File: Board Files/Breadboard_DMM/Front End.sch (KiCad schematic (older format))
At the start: 35 parts

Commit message: Started cleaning up front end page
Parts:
- removed C?: 1uF, symbol Device:C
- removed R?: 10k, symbol Device:R_US
- removed U?: 74VHC4052AFT, Package_SO:TSSOP-16_4.4x5mm_P0.65mm, symbol irex_Analog_Switch:74VHC4052AFT
- K? (x8): symbol irex_Relay:EC2-5NU_separated -> irex_Relay:EC2-5NU_Split
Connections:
- net labels added: CURRENT_SOURCE_ON, METER_CURRENT_SOURCE
- net labels removed: OHMETER_CURRENT_SOURCE, OHMETER_ON
- wire segments 134 -> 110
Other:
- note added: "Input divider"
- note removed: "0"
- note removed: "1"
- note removed: "4.096V"
- note removed: "A"
- note removed: "B\n"
- note removed: "Calibration Mux"
- note removed: "Connection"
- note removed: "GND"
- note removed: "Inputs Shorted"
- note removed: "Voltmeter \ninput divider"
- moved on the sheet: D?, R?, U?B

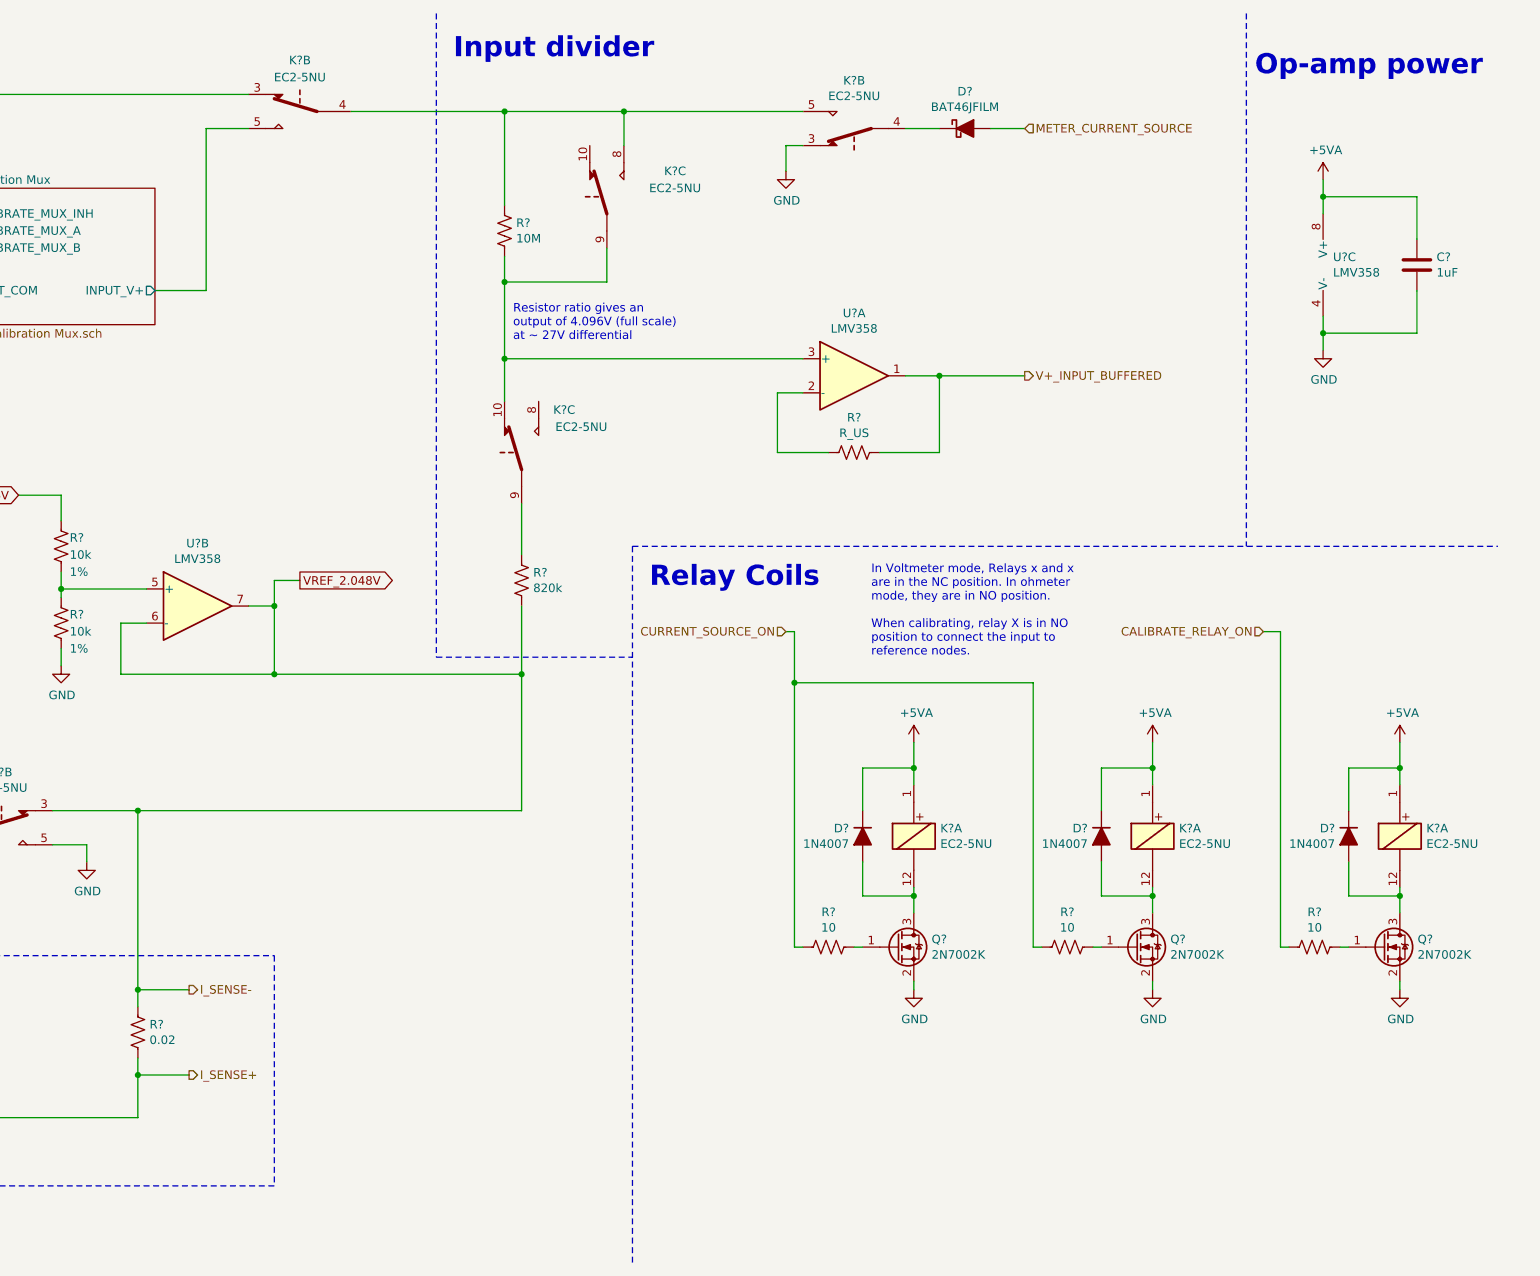
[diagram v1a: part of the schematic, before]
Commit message: Starting converting to hierachichal design
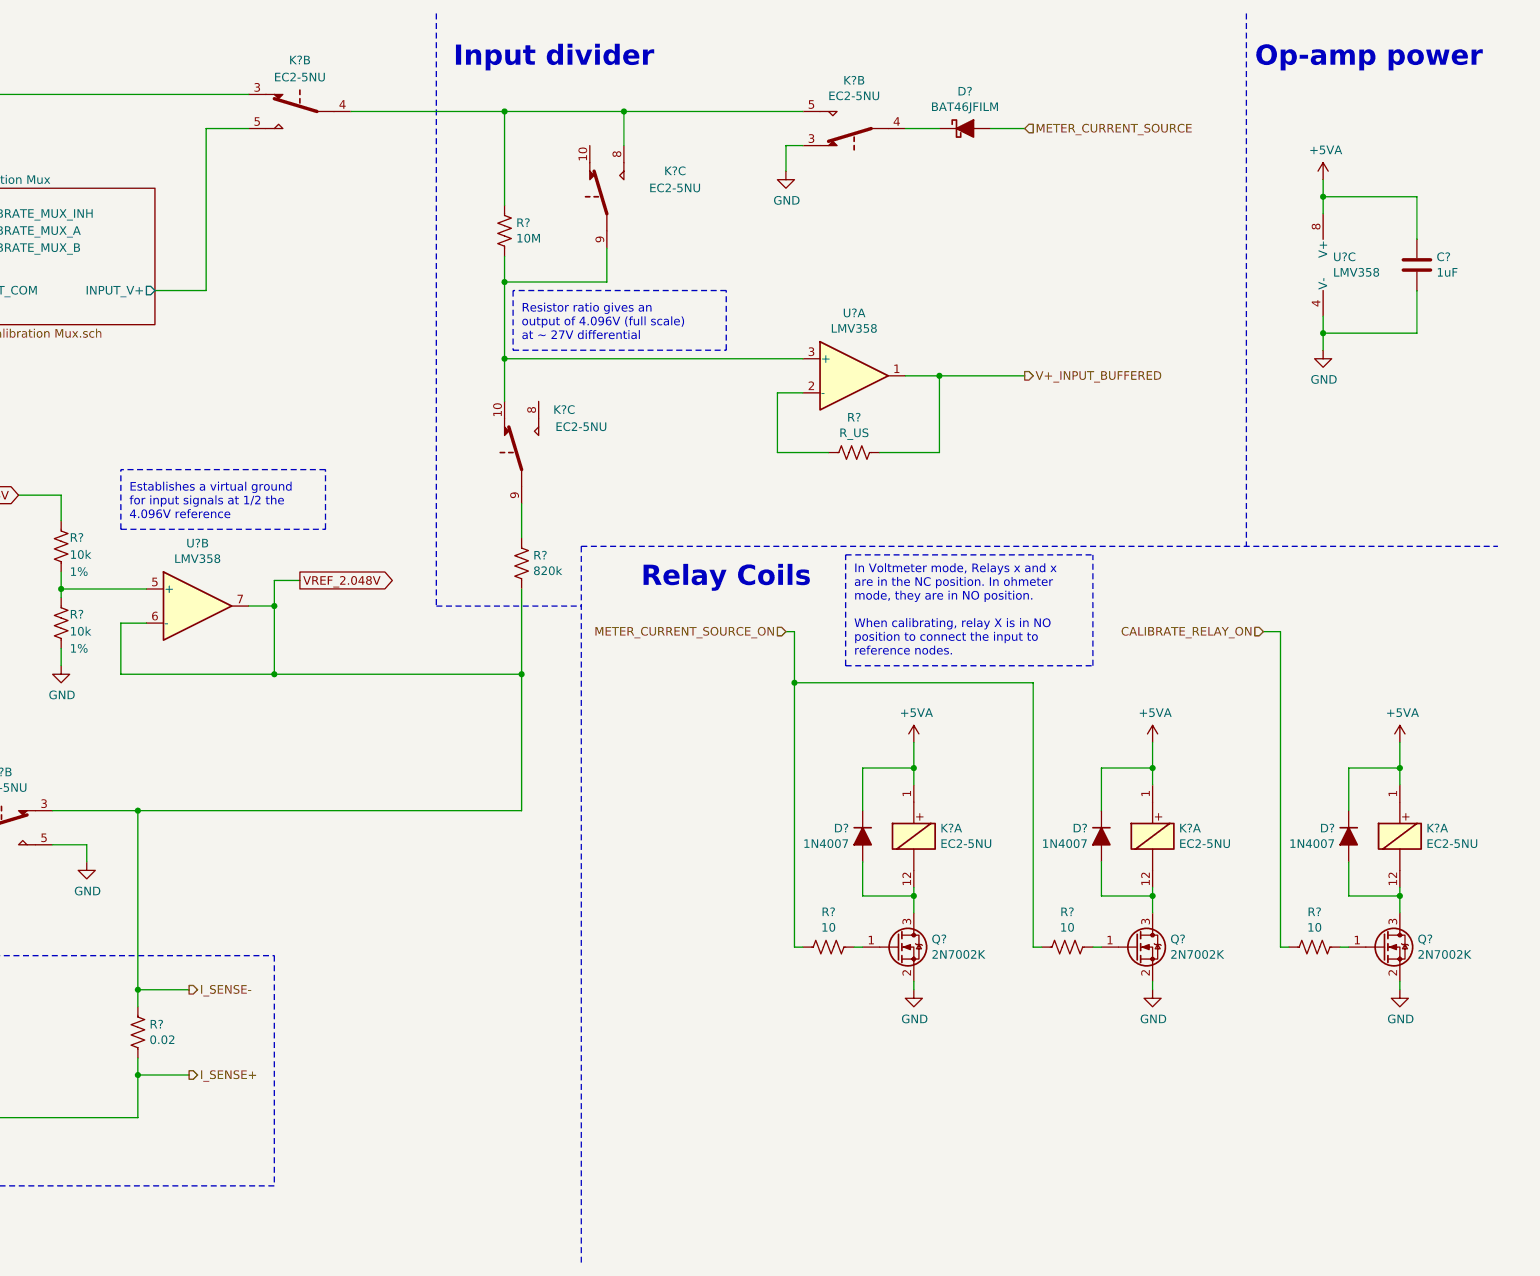
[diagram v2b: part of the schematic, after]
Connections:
- net CURRENT_SOURCE_ON renamed METER_CURRENT_SOURCE_ON
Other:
- note added: "Establishes a virtual ground \nfor input signals at 1/2 the \n4.096V reference\n"
- moved on the sheet: R?
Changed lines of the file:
@@
 $Descr A4 11693 8268
 encoding utf-8
-Sheet 2 6
+Sheet 4 6
 Title ""
 Date ""
@@
 	1    0    0    -1
 $EndComp
-Text Notes 5450 2400 0    50   ~ 0
+Text Notes 5500 2400 0    50   ~ 0
 Resistor ratio gives an \noutput of 4.096V (full scale)\nat ~~ 27V differential
 $Comp
 L Device:R_US R?
 U 1 1 5F569319
-P 5500 3800
+P 5500 3700
 AR Path="/5F569319" Ref="R?"  Part="1"
 AR Path="/5F511849/5F569319" Ref="R?"  Part="1"
-F 0 "R?" H 5568 3846 50  0000 L CNN
-F 1 "820k" H 5568 3755 50  0000 L CNN
-F 2 "" V 5540 3790 50  0001 C CNN
-F 3 "~" H 5500 3800 50  0001 C CNN
-	1    5500 3800
+F 0 "R?" H 5568 3746 50  0000 L CNN
+F 1 "820k" H 5568 3655 50  0000 L CNN
+F 2 "" V 5540 3690 50  0001 C CNN
+F 3 "~" H 5500 3700 50  0001 C CNN
+	1    5500 3700
 	1    0    0    -1
 $EndComp
@@
 $EndComp
 Wire Wire Line
-	5500 3950 5500 4350
+	5500 3850 5500 4350
 Wire Wire Line
 	2750 5150 3250 5150
@@
 	2950 5350 2950 5450
 Wire Wire Line
-	5500 3650 5500 3350
+	5500 3550 5500 3350
 Wire Wire Line
 	5400 2750 5400 2500
@@
 Connection ~ 7950 2600
 Wire Notes Line
-	6150 3600 11225 3600
+	5850 3600 11225 3600
 Wire Notes Line
 	9750 475  9750 3600
-Text Notes 9800 850  0    118  ~ 24
+Text Notes 9800 800  0    118  ~ 24
 Op-amp power\n
-Text Notes 6250 3850 0    118  ~ 24
+Text Notes 6200 3850 0    118  ~ 24
 Relay Coils
 Wire Notes Line
@@
 Connection ~ 3250 6200
 Connection ~ 3250 5150
-Text Notes 7550 4250 0    50   ~ 0
+Text Notes 7450 4250 0    50   ~ 0
 In Voltmeter mode, Relays x and x\nare in the NC position. In ohmeter\nmode, they are in NO position. \n\nWhen calibrating, relay X is in NO\nposition to connect the input to \nreference nodes.
 Text Label 1350 5250 0    50   ~ 0
@@
 Text Label 1350 6950 0    50   ~ 0
 INPUT_I+
-Text Notes 5100 750  0    118  ~ 24
+Text Notes 5100 800  0    118  ~ 24
 Input divider
 $Comp
@@
 V+_INPUT_BUFFERED
 Text HLabel 7050 4100 0    50   Input ~ 0
-CURRENT_SOURCE_ON
+METER_CURRENT_SOURCE_ON
 Text HLabel 9850 4100 0    50   Input ~ 0
 CALIBRATE_RELAY_ON
 Wire Notes Line
-	5000 475  5000 4250
+	5000 475  5000 3950
 Wire Notes Line
-	5000 4250 6150 4250
+	5000 3950 5850 3950
 Wire Wire Line
 	3250 5150 5500 5150
@@
 	5500 4350 5500 5150
 Wire Notes Line
-	6150 3600 6150 7800
+	5850 3600 5850 7800
 Text HLabel 3550 6200 2    50   Output ~ 0
 I_SENSE-
 Text HLabel 3550 6700 2    50   Output ~ 0
 I_SENSE+
+Text Notes 3200 3450 0    50   ~ 0
+Establishes a virtual ground \nfor input signals at 1/2 the \n4.096V reference\n
+Wire Notes Line width 8 style solid
+	5450 2100 5450 2450
+Wire Notes Line width 8 style solid
+	5450 2450 6700 2450
+Wire Notes Line width 8 style solid
+	6700 2450 6700 2100
+Wire Notes Line width 8 style solid
+	6700 2100 5450 2100
+Wire Notes Line width 8 style solid
+	7400 4300 8850 4300
+Wire Notes Line width 8 style solid
+	8850 4300 8850 3650
+Wire Notes Line width 8 style solid
+	7400 3650 8850 3650
+Wire Notes Line width 8 style solid
+	7400 4300 7400 3650
+Wire Notes Line width 8 style solid
+	3150 3500 4350 3500
+Wire Notes Line width 8 style solid
+	4350 3500 4350 3150
+Wire Notes Line width 8 style solid
+	4350 3150 3150 3150
+Wire Notes Line width 8 style solid
+	3150 3500 3150 3150
 $EndSCHEMATC

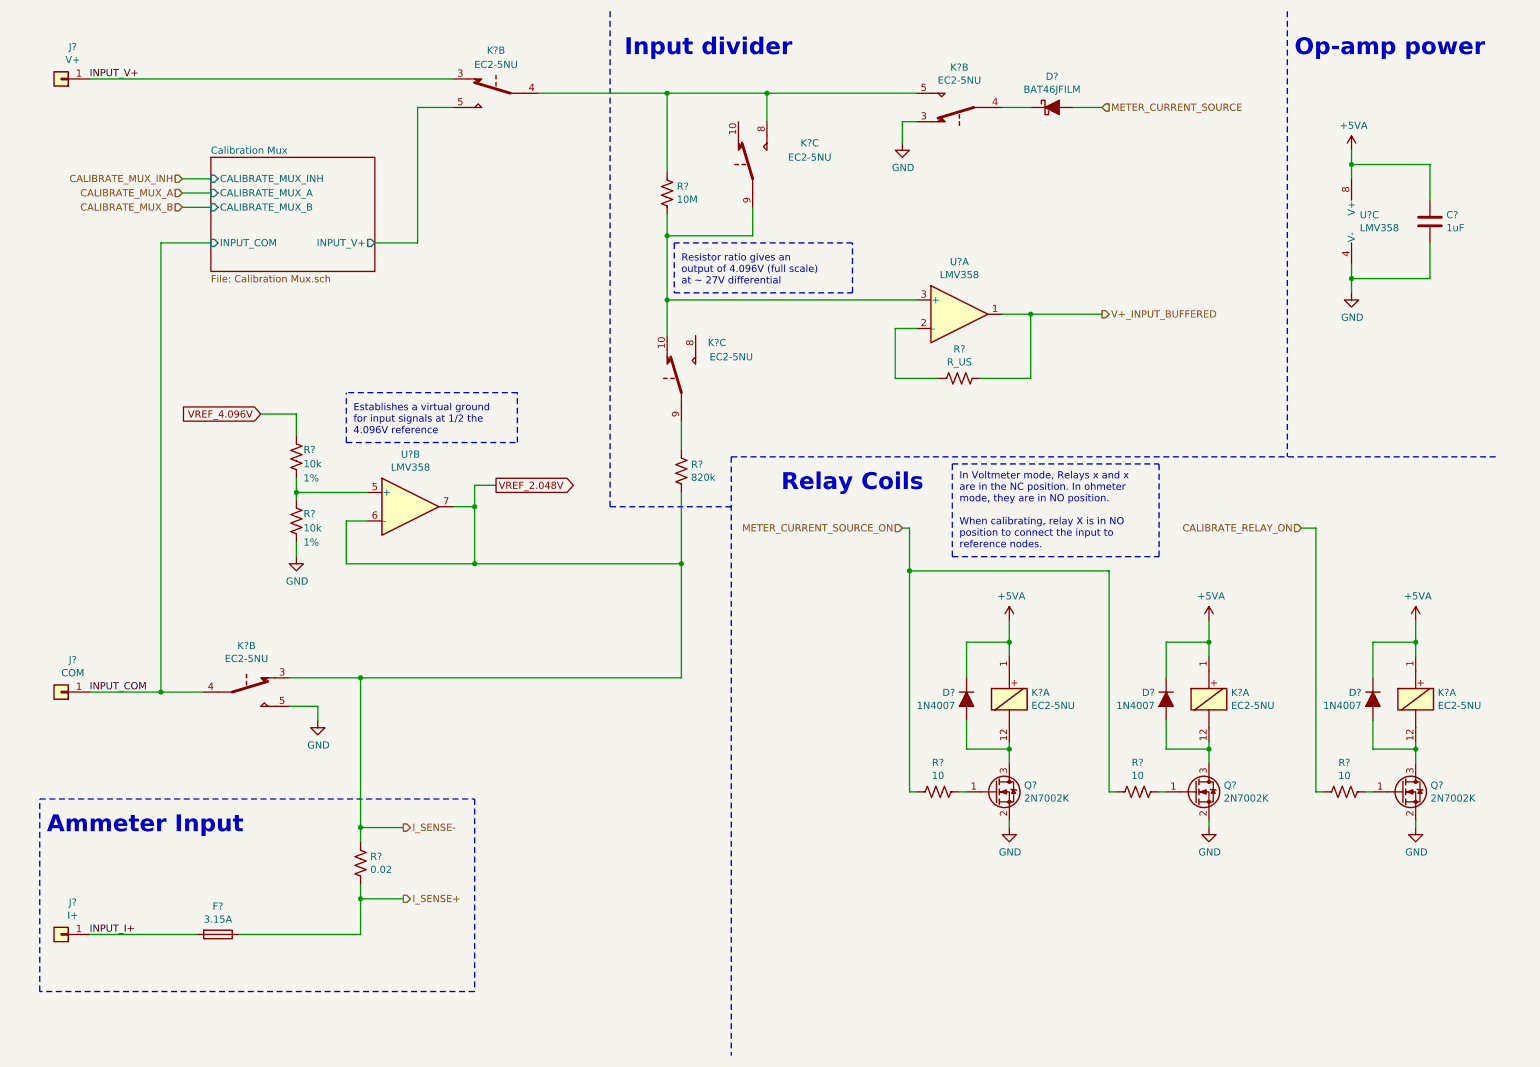
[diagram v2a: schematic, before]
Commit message: Added new sheet for main supply measurement, added upgrades document
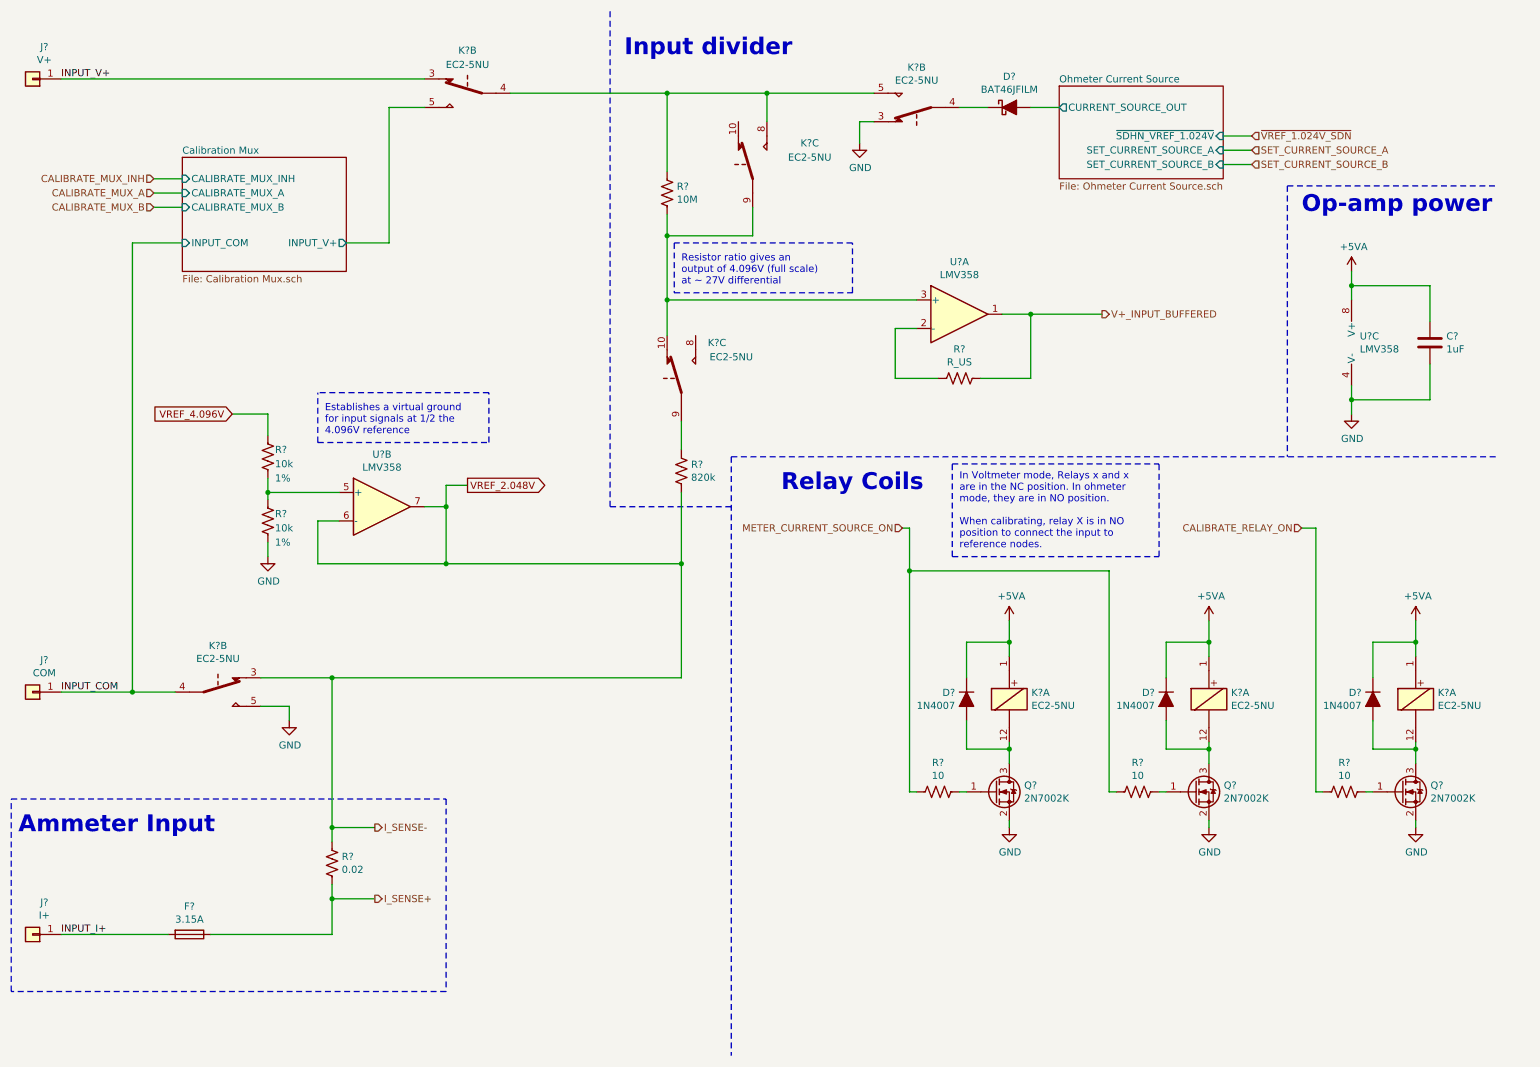
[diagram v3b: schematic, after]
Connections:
- net METER_CURRENT_SOURCE renamed Ohmeter Current Source/CURRENT_SOURCE_OUT
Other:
- moved on the sheet: C?, D?, F?, J?, K?B, R?, U?B, U?C

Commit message: Finished main design, cleaning up schematic
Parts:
- removed D?: 1N4007, Diode_SMD:D_SOD-123, symbol Device:D_ALT
- removed D?: BAT46JFILM, Diode_SMD:D_SOD-323_HandSoldering, symbol Device:D_Schottky_ALT
- removed K? (x2): EC2-5NU, Relay_THT:Relay_DPDT_Kemet_EC2, symbol irex_Relay:EC2-5NU_Split
- removed Q? (x3): 2N7002K, Package_TO_SOT_SMD:SOT-23, symbol Transistor_FET:2N7002K
- removed R?: 10, symbol Device:R_US
- added D? (x4): 1N4007, Diode_SMD:D_SOD-123, symbol Device:D_ALT
- added Q? (x2): NTZD3154N, Package_TO_SOT_SMD:SOT-563, symbol irex_Transistor_FET:NTZD3154N
- added R? (x2): 10k, symbol Device:R_US
- R?: value R_US -> 750k
- R?: value 0.02 -> 0.1
- gave numbers to parts that had none: 2
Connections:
- net GND: now also Q?.1 (S1), Q?.4 (S2), R?.2, R?.2; no longer K3.5
- net I_SENSE+: now also D?.1 (K), D?.2 (A)
- net VREF_2.048V: now also D?.1 (K), D?.2 (A)
- net at D?.2 (A), K3.12: now also Q?.3 (D2)
- net at D?.2 (A), K2.12: now also Q?.6 (D1)
- net Ohmeter Current Source/CURRENT_SOURCE_OUT+: now reaches K2.4
- net at R?.1: now also Q?.5 (G2), R?.1
- net at R?.1: now also Q?.2 (G1), R?.1
- new net: D?.1 (K), D?.1 (K), D?.2 (A), D?.2 (A)
- new net CURRENT_SOURCE_-: K3.5
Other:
- note added: "750k Here"
- note added: "In Voltmeter mode, Relays XX and XX\nare in the NC position. In ohmeter\nmode, they are in NO position. \n\nWhen calibrating, relay XX is in NO\nposition to connect the input to \nreference nodes."
- note added: "Ohmmeter Relay\nCoils"
- note added: "TODO: Clean me…I’m a mess"
- note removed: "In Voltmeter mode, Relays x and x\nare in the NC position. In ohmeter\nmode, they are in NO position. \n\nWhen calibrating, relay X is in NO\nposition to connect the input to \nreference nodes."
- note removed: "Input divider"
- note removed: "Relay Coils"
- moved on the sheet: D?, F?, J?, K2A, K3A, R?

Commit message: Finished main cleanup, started adding digikey part numbers
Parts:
- removed D? (x6): 1N4007, Diode_SMD:D_SOD-123, symbol Device:D_ALT
- removed F?: 3.15A, irex_Fuse:Fuseholder_Cylinder-5x20mm_Littlefuse_0PTF0078P_Horizontal_Open, symbol Device:Fuse
- removed unit 1 of K2
- removed unit 1 of K3
- removed Q? (x2): NTZD3154N, Package_TO_SOT_SMD:SOT-563, symbol irex_Transistor_FET:NTZD3154N
- removed R? (x2): 10, symbol Device:R_US
- removed R?: 0.1, symbol Device:R_US
- removed R? (x2): 10k, symbol Device:R_US
- added R402: 750k, symbol Device:R_US
- C401: renamed from C?; Digi-Key PN (none) -> -
- J401, J402, J403: renamed from J?; Digi-Key PN (none) -> -
- K2, K3: Digi-Key PN (none) -> -
- R401, R404: renamed from R?; Digi-Key PN (none) -> -; Tolerance (none) -> 0.1%
- R403, R405, R406: renamed from R?; Digi-Key PN (none) -> -
- U401: renamed from U?; Digi-Key PN (none) -> -
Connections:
- net INPUT_V+ is gone; now on net Calibration Mux/INPUT_V+: J401.1 (Pin_1)
- net Calibration Mux/OUTPUT_V+: now also K2.5, K2.9
- net at K3.10, R401.2, U401.3 (+): now also R402.2; no longer K2.9
- net at K2.10: now also R401.1
- net INPUT_COM renamed Ammeter Frontend/INPUT_I-
- net INPUT_I+ renamed Ammeter Frontend/INPUT_I+
- new net: K2.8, R402.1
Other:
- note added: "Front End"
- note added: "On startup, the calibration mux \nconnects the volts input to the\n4.096V reference, GND, and \n2.048V. This allows software \ncalibration for any tolerance or \noffset errors."
- note removed: "750k Here"
- note removed: "Ammeter Input"
- note removed: "Ohmmeter Relay\nCoils"
- note removed: "TODO: Clean me…I’m a mess"
- moved on the sheet: C401, J401, J402, J403, K2B, K2C, K3B, K3C, R401, R403, R404, R405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
